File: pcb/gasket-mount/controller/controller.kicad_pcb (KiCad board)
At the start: 2 copper layers, 29.6 x 25.5 mm, 34 parts, among them J1 USB_C_Receptacle_USB2.0_16P, J2 Conn_01x18_MountingPin, SW1 SW_Push, SW2 SW_Push, U1 USBLC6-2SC6, U3 W25Q128JVP, U4 RP2040, U5 AP2112K-3.3, X1 ABM8-272-T3

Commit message: gasket pcb
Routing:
- net /RESET: track 4.33 -> 1.81 mm

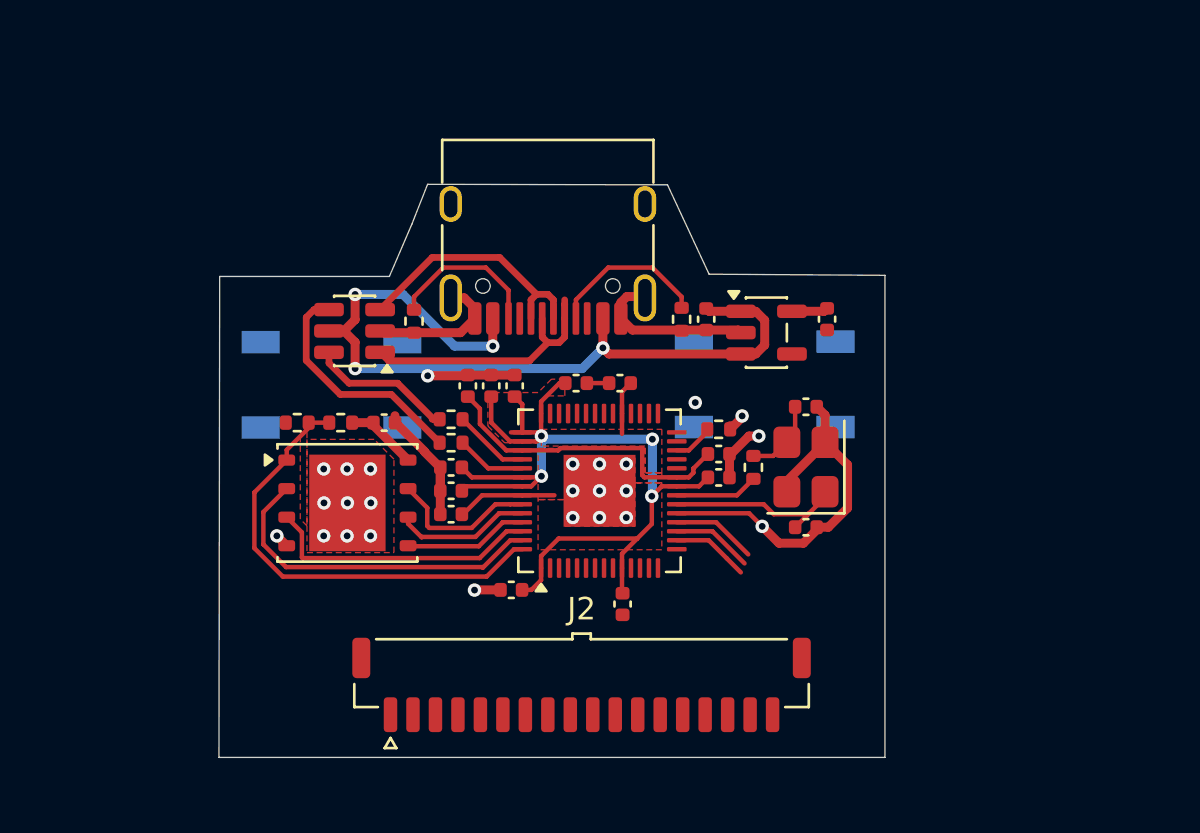
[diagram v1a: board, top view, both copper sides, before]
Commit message: Netclasses and ready for updated pcb layout
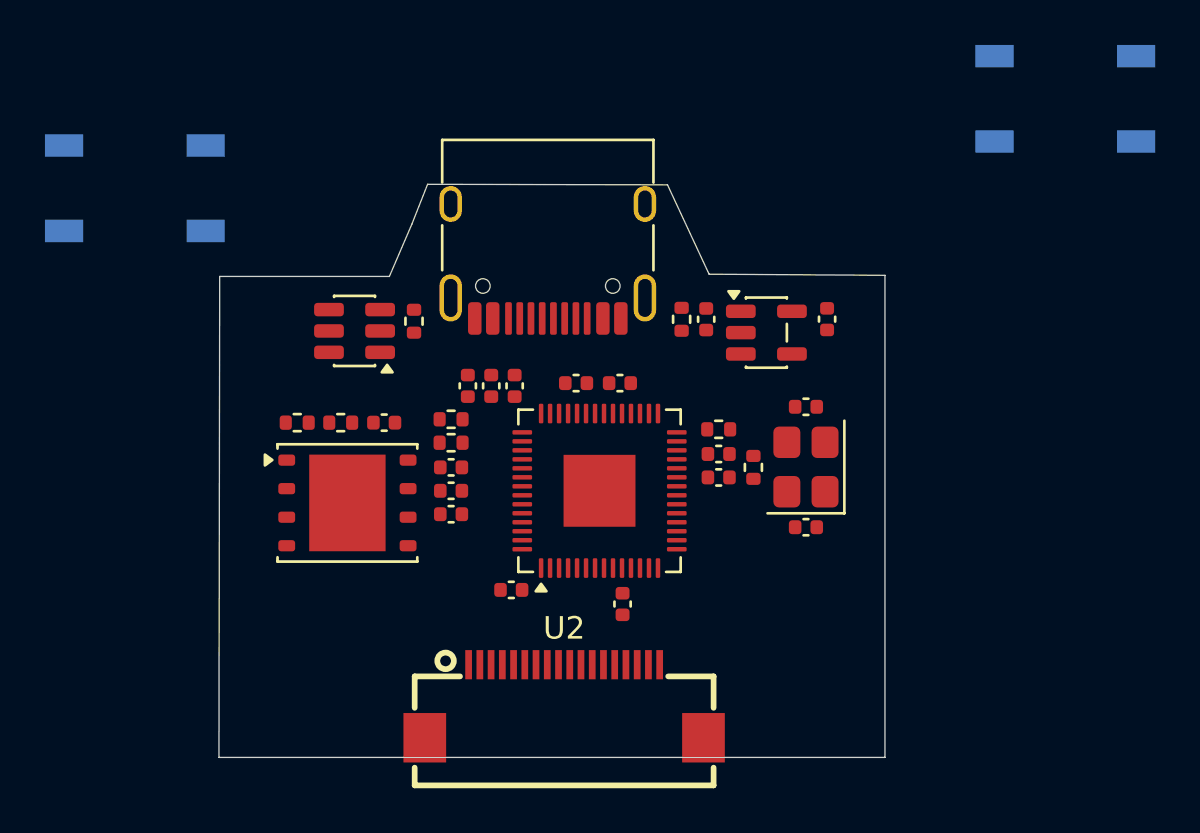
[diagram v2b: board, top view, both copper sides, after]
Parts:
- removed J2: Conn_01x18_MountingPin, Connector_Samtec_MicroMate:Samtec_T1M-18-X-S-V_1x18-1MP_P1.0mm_Terminal_Vertical
- added U2: ~, EasyEDA_Lib:FPC-SMD_18P-P0.50_TF31-18S-0.5SH-800, F.Cu at (77.6, 82.6)
- moved SW2 18.4 mm to (99.9, 55.8)
- moved SW1 12.4 mm to (58.5, 59.8)
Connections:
- net Net-(J1-D+-PadA6) renamed /USB+
- net Net-(J1-D--PadA7) renamed /USB-
- R7 pad 2: /RPD+ -> /RPD-
- R8 pad 2: /RPD- -> /RPD+
- U4 pad 11: unconnected-(U4-GPIO8-Pad11) -> COL1
- U4 pad 12: unconnected-(U4-GPIO9-Pad12) -> COL2
- U4 pad 13: unconnected-(U4-GPIO10-Pad13) -> COL3
- U4 pad 14: unconnected-(U4-GPIO11-Pad14) -> ROW1
- U4 pad 16: ROW3 -> unconnected-(U4-GPIO13-Pad16)
- U4 pad 17: COL1 -> unconnected-(U4-GPIO14-Pad17)
- U4 pad 18: COL2 -> unconnected-(U4-GPIO15-Pad18)
- U4 pad 29: COL3 -> unconnected-(U4-GPIO18-Pad29)
- U4 pad 30: ROW1 -> unconnected-(U4-GPIO19-Pad30)
- U4 pad 46: /RPD+ -> /RPD-
- U4 pad 47: /RPD- -> /RPD+
- U4 pad 9: unconnected-(U4-GPIO7-Pad9) -> ROW3
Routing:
- net +3V3: track 49.9 -> 0.00 mm, vias 5 -> 0
- net GND: track 46.2 -> 0.00 mm, vias 24 -> 0
- net VBUS: track 36.8 -> 0.00 mm, vias 4 -> 0
- net QSPI_SS: track 20.5 -> 0.00 mm
- net +1V1: track 18.3 -> 0.00 mm
- net QSPI_SD1: track 15.4 -> 0.00 mm
- net QSPI_SD2: track 12.4 -> 0.00 mm
- net /USB-: track 11.6 -> 0.00 mm
- net /USB+: track 11.5 -> 0.00 mm
- net DATA+: track 10.5 -> 0.00 mm
- net XIN: track 8.52 -> 0.00 mm
- net Net-(J1-CC1): track 7.16 -> 0.00 mm
- net Net-(J1-CC2): track 6.99 -> 0.00 mm
- net DATA-: track 6.77 -> 0.00 mm
- net QSPI_SD3: track 6.71 -> 0.00 mm
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- removed copper zone on F.Cu, net +1V1
- removed copper zone on F.Cu, net +3V3
- removed copper zone on F.Cu, net GND

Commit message: Compact form factor
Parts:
- removed SW1: SW_Push, Button_Switch_SMD:SW_SPST_TL3342
- added SW3: ~, EasyEDA_Lib:KEY-SMD_4P-L4.2-W3.2-P2.20-LS4.6, F.Cu at (73.4, 80.6)
- SW2: value SW_Push -> ~; footprint Button_Switch_SMD:SW_SPST_TL3342 -> EasyEDA_Lib:KEY-SMD_4P-L4.2-W3.2-P2.20-LS4.6; moved to F.Cu
- moved SW2 33.4 mm to (73.4, 76.0), turned to 180 degrees
- moved C3 17.2 mm to (73.9, 73.2), turned to 180 degrees
- moved R3 16.8 mm to (81.3, 79.9), turned to 135 degrees
- moved R4 16.5 mm to (80.0, 78.6), turned to -45 degrees
- moved U5 14.0 mm to (73.3, 70.5), turned to -90 degrees
- moved U3 13.7 mm to (81.6, 75.3), turned to 135 degrees
- moved U2 13.4 mm to (91.0, 80.8)
- moved C9 11.6 mm to (86.8, 75.9), turned to -90 degrees
- moved C12 11.5 mm to (84.5, 65.6)
- moved C13 11.4 mm to (85.4, 65.6)
- moved C14 11.3 mm to (86.4, 65.6)
- moved C11 11.1 mm to (83.3, 71.2)
- moved R5 11.1 mm to (96.6, 68.7), turned to -135 degrees
- moved C16 11.1 mm to (83.3, 70.2)
- moved C17 11.1 mm to (83.3, 69.2)
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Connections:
- SW2 pad 1: GND -> /BOOT
- SW2 pad 2: /RESET -> /BOOT
- U2 pad 1: unconnected-(U2-Pad1) -> GND
- U2 pad 10: unconnected-(U2-Pad10) -> COL1
- U2 pad 11: unconnected-(U2-Pad11) -> COL2
- U2 pad 12: unconnected-(U2-Pad12) -> COL3
- U2 pad 13: unconnected-(U2-Pad13) -> ROW1
- U2 pad 14: unconnected-(U2-Pad14) -> ROW2
- U2 pad 15: unconnected-(U2-Pad15) -> COL6
- U2 pad 16: unconnected-(U2-Pad16) -> COL7
- U2 pad 17: unconnected-(U2-Pad17) -> COL4
- U2 pad 18: unconnected-(U2-Pad18) -> GND
- U2 pad 19: unconnected-(U2-Pad19) -> GND
- U2 pad 2: unconnected-(U2-Pad2) -> COL5
- U2 pad 20: unconnected-(U2-Pad20) -> GND
- U2 pad 3: unconnected-(U2-Pad3) -> COL12
- U2 pad 4: unconnected-(U2-Pad4) -> COL11
- U2 pad 5: unconnected-(U2-Pad5) -> COL10
- U2 pad 6: unconnected-(U2-Pad6) -> COL8
- U2 pad 7: unconnected-(U2-Pad7) -> COL9
- U2 pad 8: unconnected-(U2-Pad8) -> ROW4
- U2 pad 9: unconnected-(U2-Pad9) -> ROW3
- U4 pad 15: unconnected-(U4-GPIO12-Pad15) -> ROW2
- U4 pad 16: unconnected-(U4-GPIO13-Pad16) -> COL6
- U4 pad 17: unconnected-(U4-GPIO14-Pad17) -> COL7
- U4 pad 18: unconnected-(U4-GPIO15-Pad18) -> COL4
- U4 pad 31: ROW2 -> unconnected-(U4-GPIO20-Pad31)
- U4 pad 35: COL6 -> unconnected-(U4-GPIO23-Pad35)
- U4 pad 36: COL7 -> unconnected-(U4-GPIO24-Pad36)
- U4 pad 38: COL4 -> unconnected-(U4-GPIO26/ADC0-Pad38)
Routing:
- net GND: track 0.00 -> 19.7 mm, vias 0 -> 1
- net +3V3: track 0.00 -> 18.6 mm
- net VBUS: track 0.00 -> 16.4 mm
- net QSPI_SS: track 0.00 -> 11.3 mm
- net QSPI_SD3: track 0.00 -> 9.25 mm
- net /BOOT: track 0.00 -> 8.76 mm
- net DATA+: track 0.00 -> 8.61 mm
- net COL4: track 0.00 -> 8.24 mm
- net QSPI_SD1: track 0.00 -> 8.09 mm
- net +1V1: track 0.00 -> 7.92 mm
- net QSPI_SCLK: track 0.00 -> 7.66 mm
- net COL7: track 0.00 -> 7.62 mm
- net Net-(J1-CC1): track 0.00 -> 7.12 mm
- net COL6: track 0.00 -> 7.00 mm
- net Net-(J1-CC2): track 0.00 -> 6.99 mm
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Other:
- board size 29.6 x 25.5 mm -> 31.3 x 24.9 mm

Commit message: Last commit before changing Flash memory
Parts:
- added H1: MountingHole_Pad, MountingHole:MountingHole_2.2mm_M2_ISO14580_Pad, F.Cu at (83.0, 78.8)
- added H2: MountingHole_Pad, MountingHole:MountingHole_2.2mm_M2_ISO14580_Pad, F.Cu at (84.0, 61.1)
- added H3: MountingHole_Pad, MountingHole:MountingHole_2.2mm_M2_ISO14580_Pad, F.Cu at (101.8, 61.2)
- moved SW3 5.15 mm to (77.2, 77.1), turned to -90 degrees
- moved C16 4.83 mm to (86.3, 66.4)
- moved C5 4.83 mm to (102.4, 65.6)
- moved R5 4.83 mm to (99.7, 65.0)
- moved C17 4.83 mm to (86.3, 65.4)
- moved C6 4.83 mm to (97.4, 66.0)
- moved R3 4.83 mm to (84.4, 76.2)
- moved U2 4.83 mm to (94.0, 77.1)
- moved U4 4.83 mm to (92.2, 67.0)
- moved C4 4.83 mm to (98.6, 69.3)
- moved R8 4.83 mm to (86.3, 64.4)
- moved X1 4.83 mm to (100.5, 67.4)
- moved C14 4.83 mm to (89.4, 61.8)
- moved C15 4.83 mm to (90.3, 61.8)
- moved C7 4.83 mm to (93.3, 61.8)
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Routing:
- net /BOOT: track 8.76 -> 0.00 mm
- net DATA+: track 8.61 -> 13.8 mm
- net DATA-: track 6.08 -> 11.2 mm
- net /RESET: track 6.14 -> 1.94 mm
- net GND: track 19.7 -> 22.4 mm, vias 1 -> 2
- net +3V3: track 18.6 -> 20.3 mm
- added copper zone on B.Cu, net GND
- added copper zone on F.Cu, net GND
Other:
- board size 31.3 x 24.9 mm -> 34.7 x 22.3 mm

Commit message: new flash
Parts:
- removed C1: 100n, Capacitor_SMD:C_0402_1005Metric
- removed H2: MountingHole_Pad, MountingHole:MountingHole_2.2mm_M2_ISO14580_Pad
- removed R3: 10k, Resistor_SMD:R_0402_1005Metric
- removed R4: 1k, Resistor_SMD:R_0402_1005Metric
- removed SW2: ~, EasyEDA_Lib:KEY-SMD_4P-L4.2-W3.2-P2.20-LS4.6
- removed U3: W25Q128JVP, Package_SON:WSON-8-1EP_6x5mm_P1.27mm_EP3.4x4.3mm
- added C18: 100n, Capacitor_SMD:C_0402_1005Metric, F.Cu at (77.5, 74.5)
- added R10: 10k, Resistor_SMD:R_0402_1005Metric, F.Cu at (77.5, 76.5)
- added R9: 1k, Resistor_SMD:R_0402_1005Metric, F.Cu at (77.5, 78.5)
- added SW4: ~, EasyEDA_Lib:KEY-SMD_4P-L4.2-W3.2-P2.20-LS4.6, F.Cu at (73.8, 76.6)
- added U6: ~, EasyEDA_Lib:USON-8_L3.0-W2.0-P0.50-BL-EP, F.Cu at (79.3, 76.5)
- moved H1 12.4 mm to (72.1, 84.8)
- moved R5 12.2 mm to (90.5, 73.0), turned to 180 degrees
- moved C5 10.6 mm to (93.2, 70.9), turned to 0 degrees
- moved U2 10.3 mm to (85.6, 83.1)
- moved X1 9.50 mm to (93.2, 73.5), turned to 90 degrees
- moved C11 9.16 mm to (79.4, 73.4)
- moved C12 9.16 mm to (80.6, 67.8)
- moved C13 9.16 mm to (81.5, 67.8)
- moved C16 9.16 mm to (79.4, 72.4)
- moved C17 9.16 mm to (79.4, 71.4)
- moved C6 9.16 mm to (90.5, 72.0)
- moved C9 9.16 mm to (82.9, 78.1)
- moved R6 9.16 mm to (90.5, 70.0)
- moved U4 9.16 mm to (85.3, 72.9)
- moved C15 9.16 mm to (83.4, 67.8)
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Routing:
- net +3V3: track 20.3 -> 41.4 mm, vias 0 -> 2
- net +1V1: track 7.92 -> 20.3 mm
- net DATA-: track 11.2 -> 1.79 mm
- net DATA+: track 13.8 -> 4.57 mm
- net VBUS: track 16.4 -> 25.2 mm, vias 0 -> 2
- net /BOOT: track 0.00 -> 6.30 mm
- net QSPI_SD3: track 9.25 -> 3.69 mm
- net QSPI_SCLK: track 7.66 -> 3.03 mm
- net /RESET: track 1.94 -> 6.14 mm
- net XOUT: track 4.51 -> 1.28 mm
- net QSPI_SD0: track 5.29 -> 2.08 mm
- net GND: track 22.4 -> 20.1 mm, vias 2 -> 10
- net XIN: track 5.33 -> 7.36 mm
- net QSPI_SS: track 11.3 -> 9.58 mm
- net QSPI_SD1: track 8.09 -> 6.89 mm
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- added copper zone on F.Cu, net +3V3
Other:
- board size 34.7 x 22.3 mm -> 26.1 x 28.4 mm

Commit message: Fixed USB traces
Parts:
- moved C3 18.4 mm to (89.2, 64.1), turned to -90 degrees
- moved U5 15.0 mm to (86.5, 64.6), turned to 0 degrees
- moved C2 11.1 mm to (83.8, 64.1), turned to -90 degrees
- moved SW3 6.40 mm to (73.7, 74.1), turned to 0 degrees
- moved SW4 2.54 mm to (73.7, 79.1)
- moved C8 0.10 mm to (86.3, 78.3)
- moved C9 0.10 mm to (82.9, 78.2)
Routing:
- net +3V3: track 41.4 -> 75.8 mm, vias 2 -> 8
- net /RESET: track 6.14 -> 38.8 mm, vias 0 -> 2
- net VBUS: track 25.2 -> 35.9 mm, vias 2 -> 4
- net GND: track 20.1 -> 21.1 mm, vias 10 -> 36
- net +1V1: track 20.3 -> 19.5 mm
- added copper zone on F.Cu, net +1V1

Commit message: PCB finishing touches
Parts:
- removed SW3: ~, EasyEDA_Lib:KEY-SMD_4P-L4.2-W3.2-P2.20-LS4.6
- added H3: Mount, MountingHole:MountingHole_2.2mm_M2_ISO14580_Pad, F.Cu at (72.1, 69.8)
- added J2: I2C, Connector_PinHeader_2.54mm:PinHeader_1x02_P2.54mm_Vertical, F.Cu at (93.3, 68.3)
- added J3: PWR, Connector_PinHeader_2.54mm:PinHeader_1x02_P2.54mm_Vertical, F.Cu at (85.1, 61.1)
- added SW1: ~, EasyEDA_Lib:KEY-SMD_4P-L4.2-W3.2-P2.20-LS4.6, F.Cu at (73.7, 74.1)
- H1: value MountingHole_Pad -> Mount
- H2: renamed from H3; value MountingHole_Pad -> Mount
- J1: value USB_C_Receptacle_USB2.0_16P -> TYPE-C-31-M-12
- U2: value ~ -> TF31-18S-0.5SH(800)
- renumbered SW4 to SW2
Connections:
- U2 pad 10: COL1 -> COL5
- U2 pad 11: COL2 -> COL6
- U2 pad 12: COL3 -> COL7
- U2 pad 13: ROW1 -> COL8
- U2 pad 14: ROW2 -> COL9
- U2 pad 15: COL6 -> COL10
- U2 pad 16: COL7 -> COL11
- U2 pad 17: COL4 -> COL12
- U2 pad 2: COL5 -> ROW4
- U2 pad 3: COL12 -> ROW3
- U2 pad 4: COL11 -> ROW2
- U2 pad 5: COL10 -> ROW1
- U2 pad 6: COL8 -> COL1
- U2 pad 7: COL9 -> COL2
- U2 pad 8: ROW4 -> COL3
- U2 pad 9: ROW3 -> COL4
- U4 pad 11: COL1 -> COL5
- U4 pad 12: COL2 -> COL6
- U4 pad 13: COL3 -> COL7
- U4 pad 14: ROW1 -> COL8
- U4 pad 15: ROW2 -> COL9
- U4 pad 16: COL6 -> COL10
- U4 pad 17: COL7 -> COL11
- U4 pad 18: COL4 -> COL12
- U4 pad 2: COL5 -> ROW4
- U4 pad 3: COL12 -> ROW3
- U4 pad 38: unconnected-(U4-GPIO26/ADC0-Pad38) -> GPIO26/SDA
- U4 pad 39: unconnected-(U4-GPIO27/ADC1-Pad39) -> GPIO27/SCL
- U4 pad 4: COL11 -> ROW2
- U4 pad 5: COL10 -> ROW1
- U4 pad 6: COL8 -> COL1
- U4 pad 7: COL9 -> COL2
- U4 pad 8: ROW4 -> COL3
- U4 pad 9: ROW3 -> COL4
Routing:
- net GPIO27/SCL: track 0.00 -> 11.3 mm, vias 0 -> 1
- net GPIO26/SDA: track 0.00 -> 11.0 mm, vias 0 -> 1
- net +1V1: track 19.5 -> 14.6 mm
- net COL4: track 8.23 -> 5.34 mm
- net COL7: track 7.77 -> 5.38 mm
- net COL12: track 5.84 -> 8.23 mm
- net COL11: track 5.71 -> 7.77 mm
- net COL6: track 7.32 -> 5.51 mm
- net COL10: track 5.59 -> 7.32 mm
- net COL9: track 5.42 -> 6.83 mm
- net ROW2: track 6.83 -> 5.71 mm
- net +3V3: track 75.8 -> 76.7 mm
- net ROW4: track 5.38 -> 5.95 mm
- net GND: vias 36 -> 37

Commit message: 3d model
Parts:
- moved SW2 75.8 mm to (143.2, 109.2)
- moved C10 75.7 mm to (160.1, 100.7)
- moved C14 75.7 mm to (152.1, 97.5)
- moved C15 75.7 mm to (153.0, 97.5)
- moved C2 75.7 mm to (153.4, 93.8)
- moved C3 75.7 mm to (158.8, 93.8)
- moved C6 75.7 mm to (160.1, 101.7)
- moved C7 75.7 mm to (155.9, 97.5)
- moved J3 75.7 mm to (154.7, 90.8)
- moved U4 75.7 mm to (154.9, 102.6)
- moved U6 75.7 mm to (148.9, 106.2)
- moved C13 75.7 mm to (151.1, 97.5)
- moved C16 75.7 mm to (149.0, 102.1)
- moved C18 75.7 mm to (147.1, 104.2)
- moved C4 75.7 mm to (162.8, 105.8)
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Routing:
- net /RESET: track 39.1 -> 36.9 mm
- net Net-(C5-Pad1): track 3.28 -> 2.75 mm
- net GND: track 21.1 -> 20.9 mm, vias 37 -> 42
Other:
- board size 26.1 x 28.4 mm -> 26 x 28.5 mm
- board text added: "BOOT"
- board text added: "I^{2}C"
- board text added: "PWR"
- board text added: "RESET"
- board text added: "v0"
